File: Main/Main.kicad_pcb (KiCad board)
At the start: 4 copper layers, 76.2 x 64.9 mm, 104 parts, among them J1 USB_B_Micro, J2 XT60, J3 Conn_01x03, J4 Conn_01x03, J5 Conn_01x03, J6 Conn_01x03, J7 MSD-4-A, J9 Conn_01x03, SW1 SW_Push, SW2 SW_Push, U1 RP2350A-QFN60, U10 LM75B, U11 MCS1802GS-50-Z, U12 MCS1802GS-50-Z, U13 MCS1802GS-50-Z, U14 TPS2121RUXR, U15 AP62150WU, U2 W25Q128JVS, U3 AMS1117-3.3, U4 MMC5983MA, U5 ICM-42688-P, U6 INA226, U7 KX134-1211, U8 MS5611-01BA, U9 MCS1802GS-50-Z, Y1 ABM8-272-T3

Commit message: Wiring Mostly Done
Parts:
- D2: value BLUE_LED -> YELLOW_LED
- R10, R22: value R -> 60
- moved C25 42.5 mm to (118.0, 92.2)
- moved C26 42.3 mm to (122.0, 92.2)
- moved U7 42.3 mm to (120.0, 92.0), turned to 180 degrees
- moved U5 35.3 mm to (116.0, 100.0)
- moved C30 35.1 mm to (117.0, 97.8)
- moved C29 35.0 mm to (115.0, 97.8)
- moved C22 34.3 mm to (125.0, 103.0)
- moved C23 34.3 mm to (125.0, 97.0)
- moved U4 34.3 mm to (125.0, 100.0)
- moved U8 31.2 mm to (120.0, 108.0), turned to 180 degrees
- moved C27 26.4 mm to (122.5, 109.2), turned to 90 degrees
- moved C5 0.10 mm to (104.5, 105.7)
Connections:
- C25 pad 1: IO_VDD -> +3.3V
- C26 pad 2: VDD -> +3.3V
- U1 pad 12: unconnected-(U1-GPIO8-Pad12) -> SPI_SDO
- U1 pad 14: unconnected-(U1-GPIO10-Pad14) -> SPI_SCK
- U1 pad 15: unconnected-(U1-GPIO11-Pad15) -> SPI_SDI
- U1 pad 16: unconnected-(U1-GPIO12-Pad16) -> MS5611_CS
- U1 pad 17: unconnected-(U1-GPIO13-Pad17) -> ICM_CS
- U1 pad 18: unconnected-(U1-GPIO14-Pad18) -> MMC_CS
- U1 pad 19: unconnected-(U1-GPIO15-Pad19) -> ACCEL_CS
- U1 pad 2: unconnected-(U1-GPIO0-Pad2) -> SPI_SDO2
- U1 pad 27: unconnected-(U1-GPIO16-Pad27) -> INT2/DRDY
- U1 pad 28: unconnected-(U1-GPIO17-Pad28) -> ACCEL_INT
- U1 pad 29: unconnected-(U1-GPIO18-Pad29) -> MMC_INT
- U1 pad 3: unconnected-(U1-GPIO1-Pad3) -> SD_ChipSelect
- U1 pad 31: unconnected-(U1-GPIO19-Pad31) -> PWM1
- U1 pad 34: unconnected-(U1-GPIO22-Pad34) -> PWM2
- U1 pad 35: unconnected-(U1-GPIO23-Pad35) -> PWM4
- U1 pad 36: unconnected-(U1-GPIO24-Pad36) -> PWM3
- U1 pad 4: unconnected-(U1-GPIO2-Pad4) -> SPI_SCLK2
- U1 pad 5: unconnected-(U1-GPIO3-Pad5) -> SPI_SDI2
- U1 pad 7: unconnected-(U1-GPIO4-Pad7) -> SD_CD
- U4 pad 15: unconnected-(U4-INT-Pad15) -> MMC_INT
- U4 pad 5: SPI_SD0 -> SPI_SDO
- U5 pad 1: SPI_SD0 -> SPI_SDO
- U7 pad 1: SPI_SD0 -> SPI_SDO
- U7 pad 10: ACCEL_nCS -> ACCEL_CS
- U7 pad 3: IO_VDD -> +3.3V
- U7 pad 5: ACCEL_INT1 -> ACCEL_INT
- U7 pad 6: ACCEL_INT2 -> unconnected-(U7-INT2-Pad6)
- U7 pad 7: VDD -> +3.3V
- U8 pad 6: SDO -> SPI_SDO
- U8 pad 7: SDI -> SPI_SDI
- U8 pad 8: SCLK -> SPI_SCK
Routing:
- net SPI_SDO: track 0.00 -> 51.6 mm
- net SPI_SCK: track 0.00 -> 45.8 mm, vias 0 -> 5
- net SPI_SDI: track 0.00 -> 44.9 mm, vias 0 -> 5
- net +3.3V: track 74.3 -> 115.5 mm, vias 19 -> 31
- net MMC_INT: track 0.00 -> 37.0 mm
- net MMC_CS: track 0.00 -> 24.2 mm, vias 0 -> 4
- net ACCEL_INT: track 0.00 -> 23.0 mm
- net PWM3: track 0.00 -> 22.2 mm, vias 0 -> 1
- net INT2/DRDY: track 0.00 -> 22.2 mm, vias 0 -> 2
- net GND: track 112.3 -> 133.6 mm, vias 63 -> 73
- net SPI_SDI2: track 2.95 -> 23.3 mm, vias 1 -> 2
- net PWM4: track 0.00 -> 20.3 mm, vias 0 -> 1
- net PWM2: track 0.00 -> 19.7 mm, vias 0 -> 1
- net MS5611_CS: track 0.00 -> 19.4 mm, vias 0 -> 2
- net ACCEL_CS: track 0.00 -> 19.4 mm, vias 0 -> 1
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
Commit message: PART NUMBERSSSSS
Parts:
- moved J1 0.10 mm to (100.0, 133.9)
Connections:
- U1 pad 37: unconnected-(U1-GPIO25-Pad37) -> LED1
- U1 pad 8: unconnected-(U1-GPIO5-Pad8) -> LED2
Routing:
- net LED2: track 0.00 -> 50.0 mm, vias 0 -> 2
- net LED1: track 0.00 -> 17.7 mm, vias 0 -> 2
- net ACCEL_CS: vias 1 -> 0
- net +3.3V: vias 31 -> 33
- added copper zone on B.Cu, net GND

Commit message: Basically Ready
Yippeeee
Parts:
- R10, R22: value 60 -> 100
- R11, R12: value R -> 100
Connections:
- H1 pad 1: (no net) -> GND
- H2 pad 1: (no net) -> GND
- H3 pad 1: (no net) -> GND
- H4 pad 1: (no net) -> GND
- J5 pad 1: PWM3 -> PWM4
- J5 pad 2: current -3 -> current -4
- J6 pad 1: PWM4 -> PWM3
- J6 pad 2: current -4 -> current -3
- U1 pad 35: PWM4 -> PWM3
- U1 pad 36: PWM3 -> PWM4
- U1 pad 42: Vout4 -> Vout3
- U1 pad 43: Vout3 -> Vout4
- U12 pad 1: current -3 -> current -4
- U12 pad 2: current -3 -> current -4
- U12 pad 7: Vout3 -> Vout4
- U13 pad 3: current -4 -> current -3
- U13 pad 4: current -4 -> current -3
- U13 pad 7: Vout4 -> Vout3
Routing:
- net Vout4: track 17.5 -> 19.5 mm
- net Vout3: track 19.5 -> 17.5 mm
- net PWM4: track 20.3 -> 22.2 mm
- net PWM3: track 22.2 -> 20.3 mm
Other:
- board text added: "+ -"
- board text added: "- s +"
- board text added: "2 1"
- board text added: "4 3"
- board text added: "AFS ELEC V2.0 2026"
- board text added: "BOOT"
- board text added: "RSET"
- board text added: "SRC PWR IND1 IND2"
- board text added: "SWD CK IO GND"

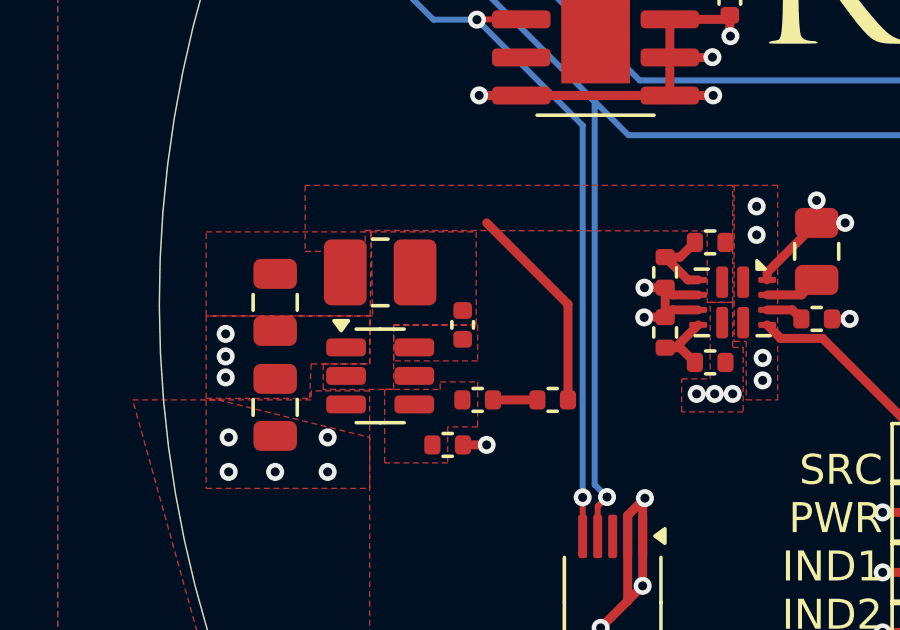
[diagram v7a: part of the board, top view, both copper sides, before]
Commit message: changed a few components for manufacturing
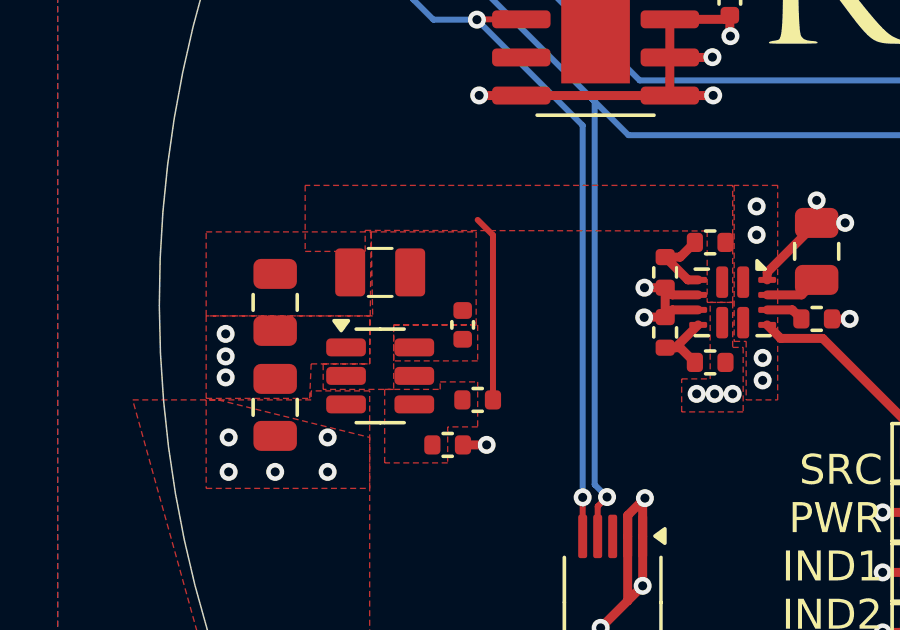
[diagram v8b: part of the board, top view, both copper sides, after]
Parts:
- removed R23: 1k, Resistor_SMD:R_0402_1005Metric
- L1: value 3.3uH -> 3.3u
- L3: footprint Inductor_SMD:L_1008_2520Metric_Pad1.43x2.20mm_HandSolder -> otherComponents:AOTA-B201610S3R3-101-T(L_0806_2016metric)
- R20: value 30k -> 47k
- R21: value 10k -> 15k
- moved R20 2.50 mm to (72.5, 103.2)
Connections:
- R20 pad 2: Net-(R20-Pad2) -> Net-(U15-FB)
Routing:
- net Net-(R20-Pad2): track 1.16 -> 0.00 mm
- net 3.3v_Batt: track 7.02 -> 6.21 mm
